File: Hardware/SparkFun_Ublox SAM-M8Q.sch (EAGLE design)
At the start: 35 parts, among them J13 Qwiic Right Angle, J3 PTH, J4 Qwiic Right Angle, U2 SAM-M8Q

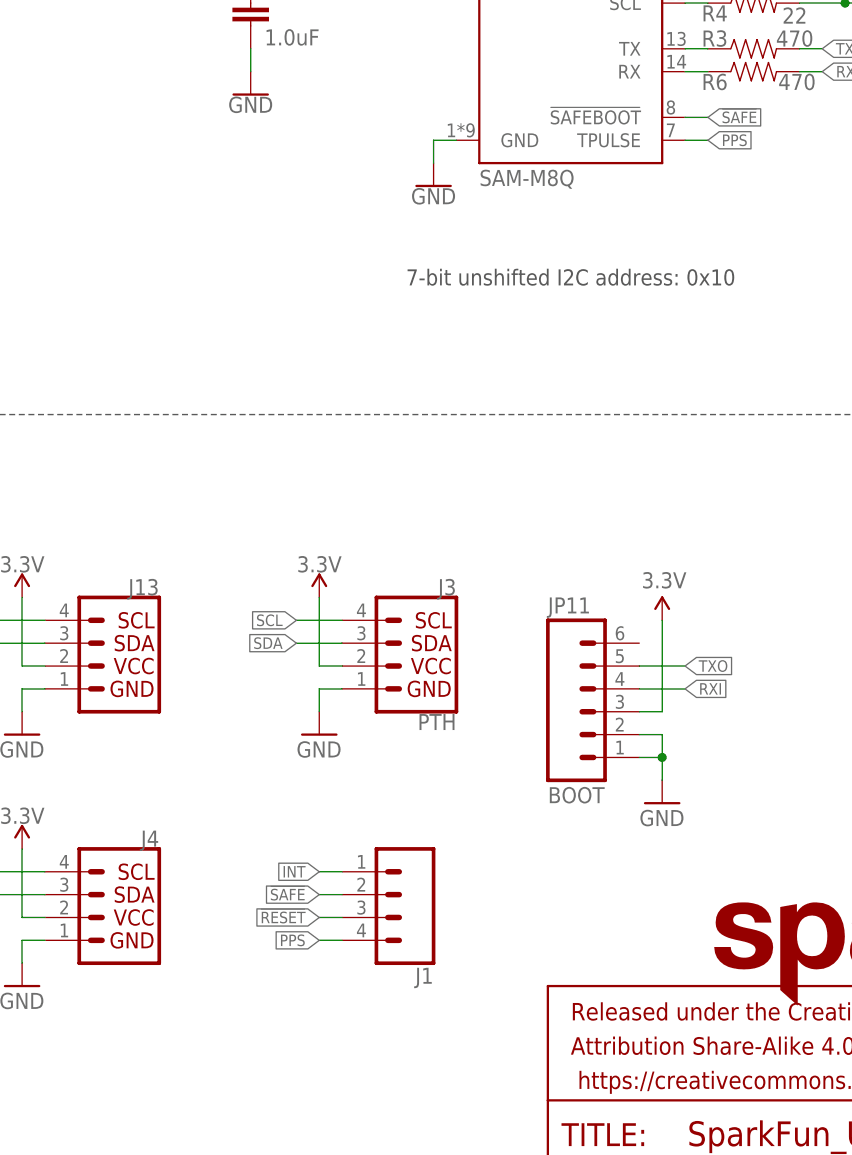
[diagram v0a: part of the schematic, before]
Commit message: Replaces all part with SparkFun parts, moves temp libarary parts to SparkFun Eagle libararies
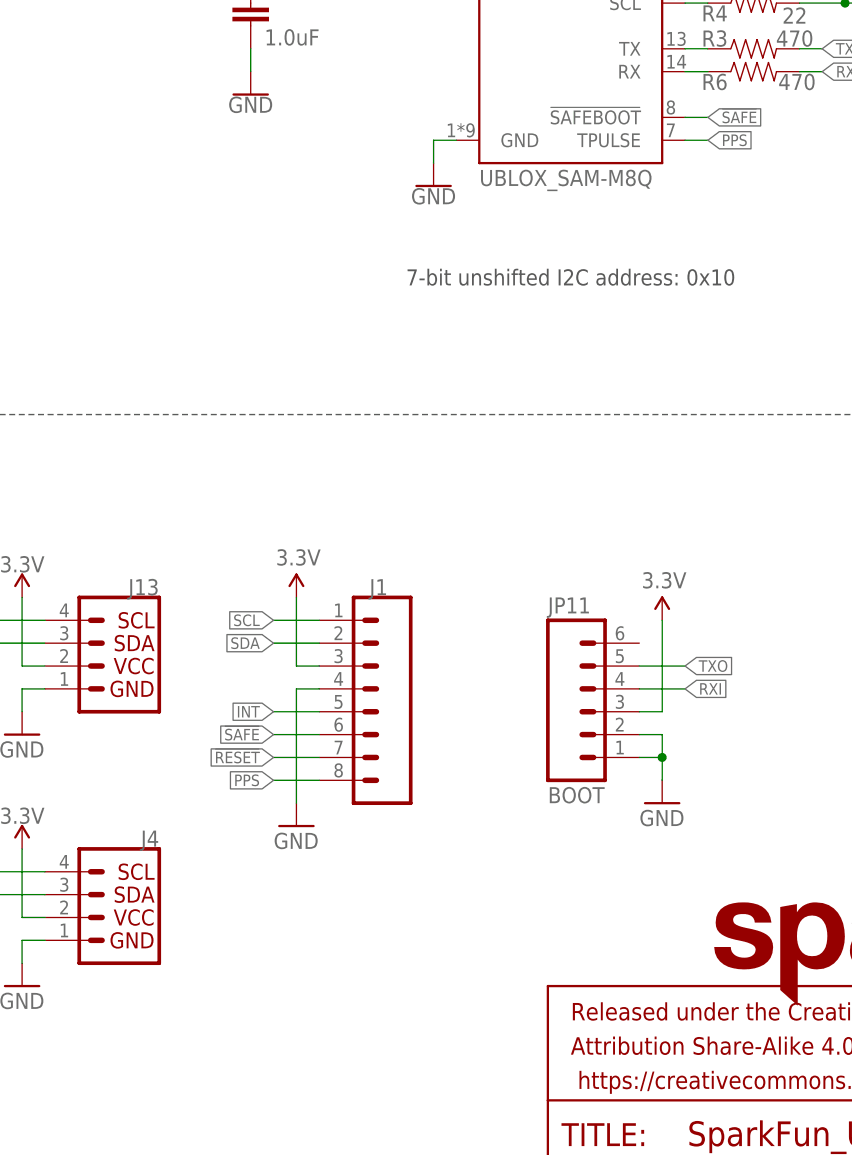
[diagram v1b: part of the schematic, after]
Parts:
- removed J3: PTH, SparkX:I2C_STANDARD_NO_SILK
- J1: device SparkFun-Connectors:CONN_041X04_NO_SILK -> SparkFun-Connectors:CONN_08NO_SILK_FEMALE_PTH
- JP10, JP3, JP4, JP9: device SparkFun:STAND-OFF -> SparkFun-Hardware:STAND-OFF
- JP11: device SparkFun-Connectors:M06NO_SILK_FEMALE_PTH -> SparkFun-Connectors:CONN_06NO_SILK_NO_POP
- JP2, JP6, JP7, JP8: device SparkFun:FIDUCIALUFIDUCIAL -> SparkFun-Aesthetics:FIDUCIALUFIDUCIAL
- U2: value SAM-M8Q -> UBLOX_SAM-M8Q; device SAM-M8Q:SAM-M8Q -> SparkFun-GPS:UBLOX_SAM-M8Q
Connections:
- net !RESET: now also J1.7; no longer J1.3
- net !SAFE: now also J1.6; no longer J1.2
- net 3.3V: now also J1.3; no longer J3.VCC
- net GND: now also J1.4; no longer J3.GND
- net INT: now also J1.5; no longer J1.1
- net PPS: now also J1.8; no longer J1.4
- net SCL: now also J1.1; no longer J3.SCL
- net SDA: now also J1.2; no longer J3.SDA

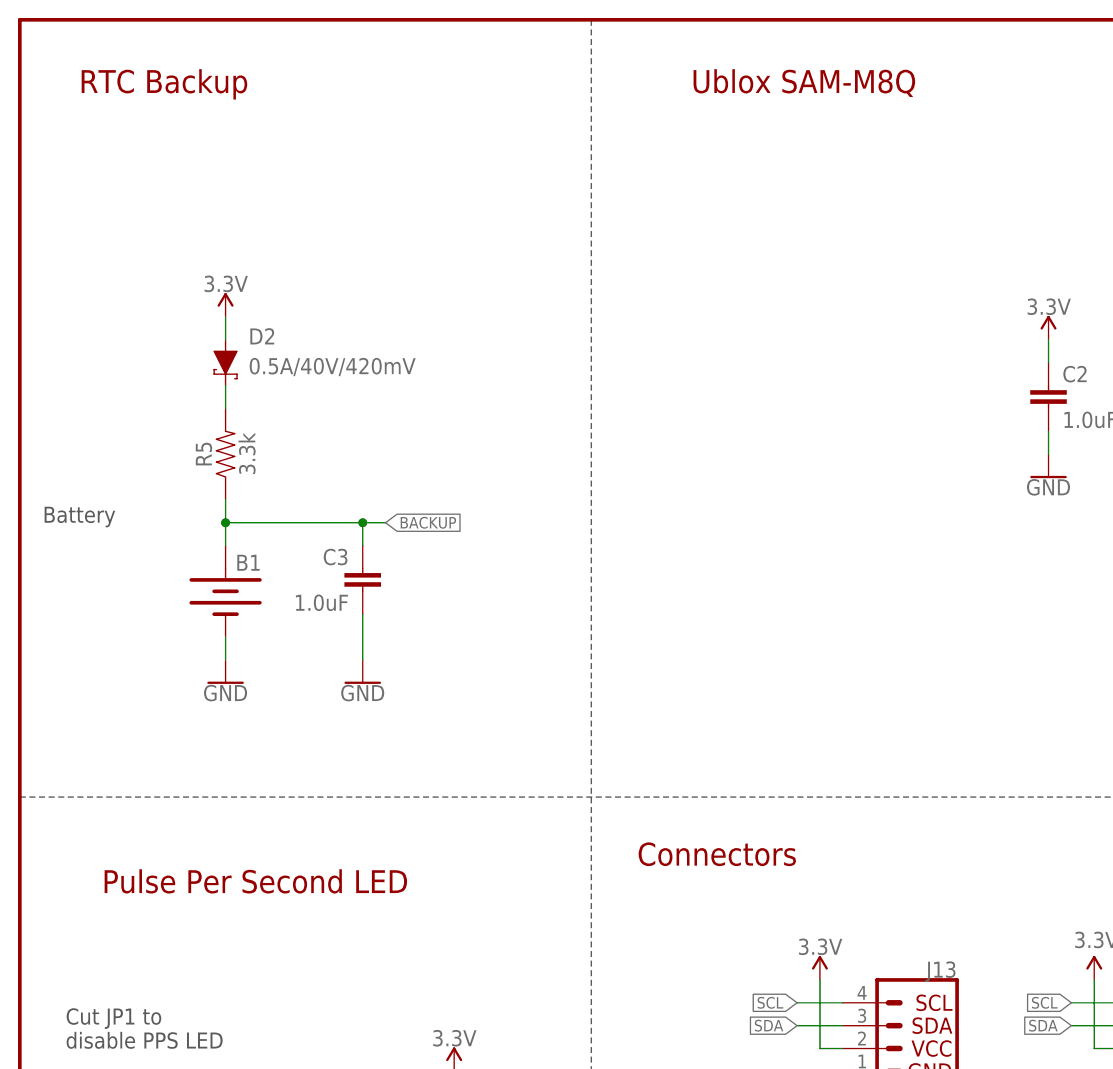
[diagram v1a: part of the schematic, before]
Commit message: Changes all drill sizes to 15 mil, adjust schematic labels
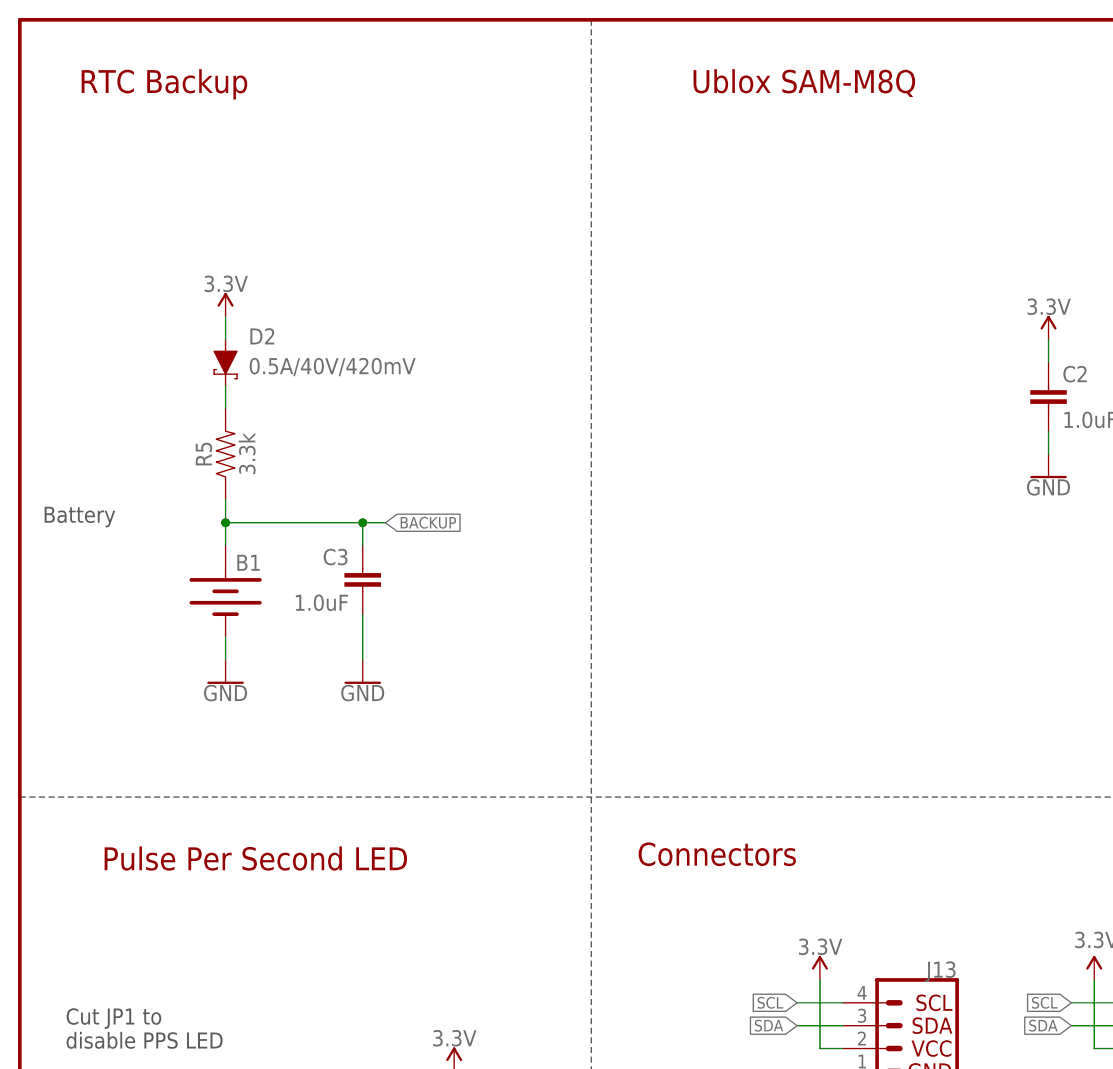
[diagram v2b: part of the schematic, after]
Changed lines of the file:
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@@
 <text x="237.744" y="7.366" size="2.54" layer="94" font="vector">v10</text>
 <text x="149.86" y="114.3" size="1.778" layer="97" font="vector" align="center">7-bit unshifted I2C address: 0x10</text>
-<text x="87.122" y="178.562" size="2.54" layer="94" font="vector" ratio="15" rot="MR180" align="center">Ublox SAM-M8Q</text>
-<text x="16.002" y="178.562" size="2.54" layer="94" font="vector" ratio="15" rot="MR180" align="center">RTC Backup</text>
-<text x="26.162" y="89.662" size="2.54" layer="94" font="vector" ratio="15" rot="MR180" align="center">Pulse Per Second LED</text>
+<text x="87.122" y="178.562" size="2.54" layer="94" font="vector" ratio="12" rot="MR180" align="center">Ublox SAM-M8Q</text>
+<text x="16.002" y="178.562" size="2.54" layer="94" font="vector" ratio="12" rot="MR180" align="center">RTC Backup</text>
+<text x="26.162" y="92.202" size="2.54" layer="94" font="vector" ratio="12" rot="MR180" align="center">Pulse Per Second LED</text>
 <wire x1="0" y1="99.06" x2="248.92" y2="99.06" width="0.1524" layer="97" style="shortdash"/>
 <wire x1="63.5" y1="185.42" x2="63.5" y2="0" width="0.1524" layer="97" style="shortdash"/>
